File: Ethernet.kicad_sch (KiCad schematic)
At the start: 40 parts, among them U4 LAN8742A

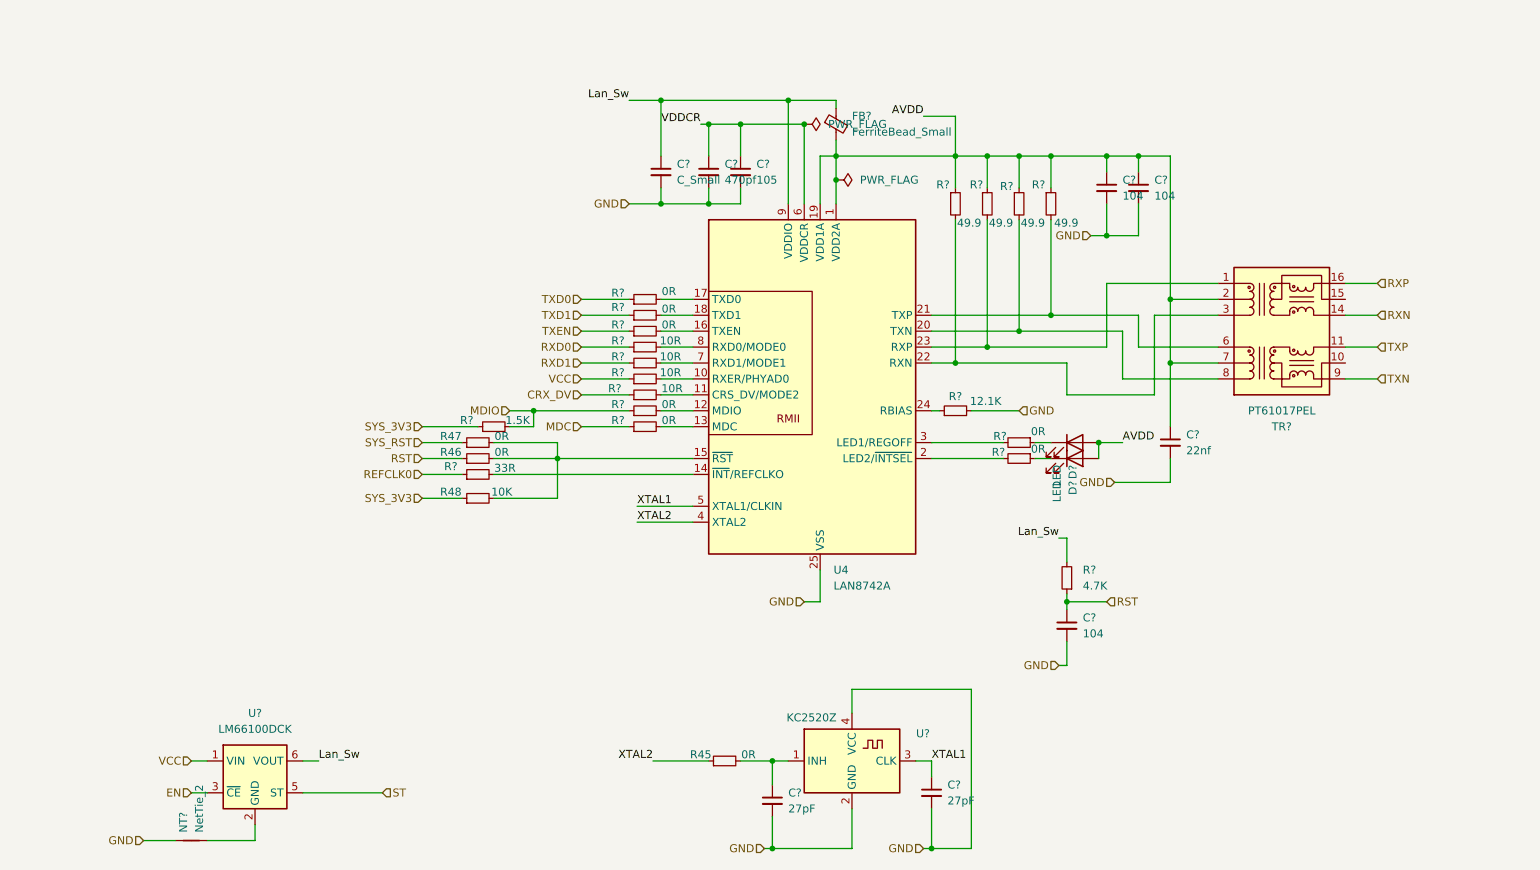
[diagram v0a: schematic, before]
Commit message: Completed ETH Module as per ref schematic also populated compatible busses in processor module
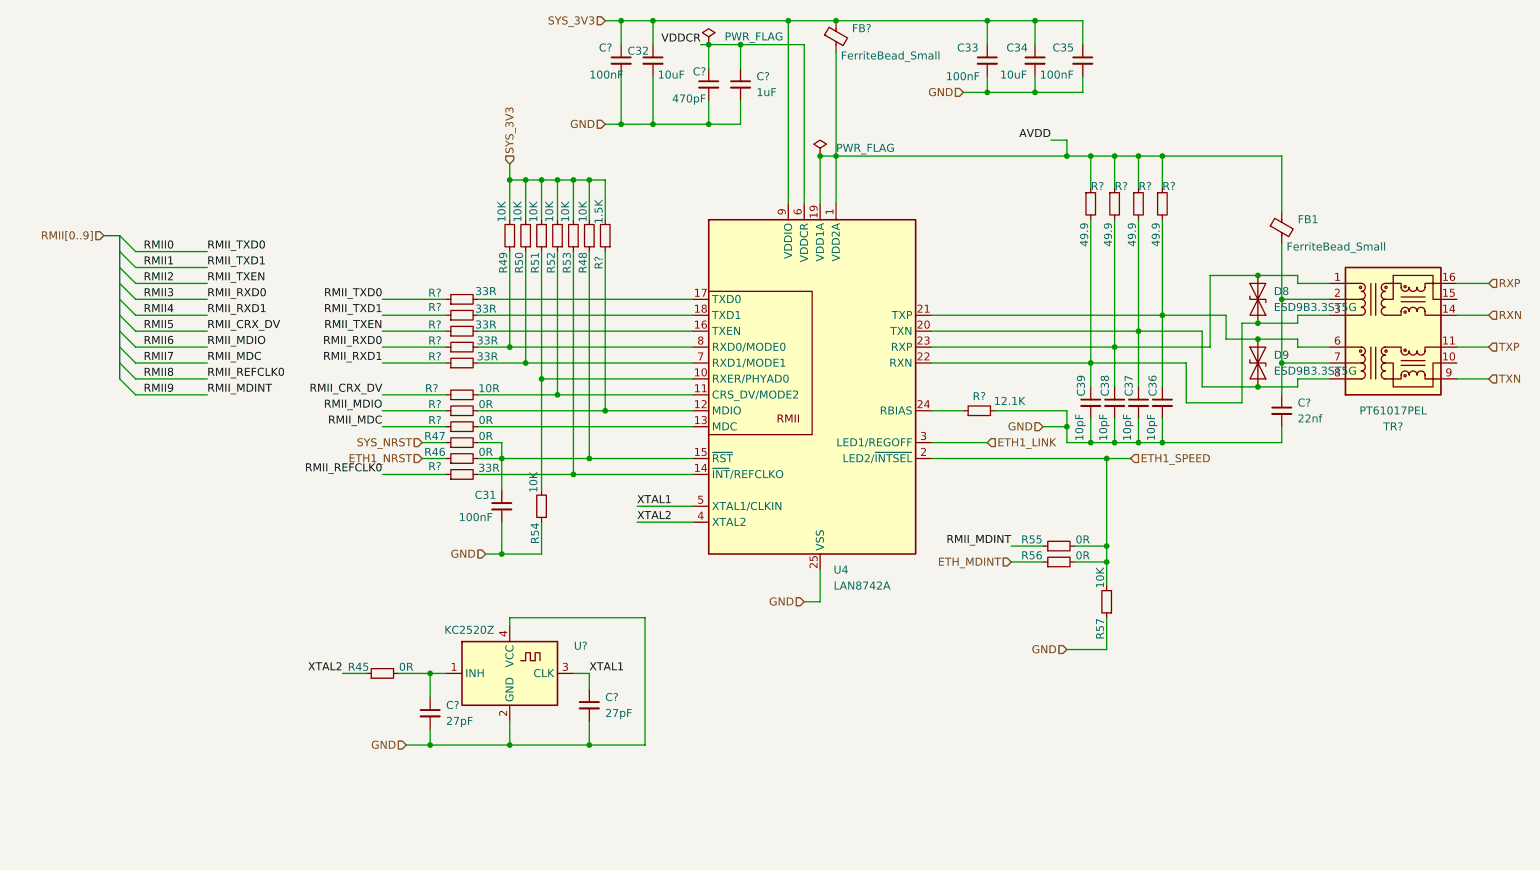
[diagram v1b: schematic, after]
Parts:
- removed C? (x3): 104, Capacitor_SMD:C_0603_1608Metric_Pad1.08x0.95mm_HandSolder, symbol Device:C_Small
- removed D? (x2): LED, LED_SMD:LED_0603_1608Metric, symbol Device:LED
- removed NT?: NetTie_2, NetTie:NetTie-2_SMD_Pad0.5mm, symbol Device:NetTie_2
- removed R? (x2): 0R, Resistor_SMD:R_0603_1608Metric_Pad0.98x0.95mm_HandSolder, symbol Device:R_Small
- removed R?: 10R, Resistor_SMD:R_0603_1608Metric_Pad0.98x0.95mm_HandSolder, symbol Device:R_Small
- removed R?: 4.7K, Resistor_SMD:R_0603_1608Metric_Pad0.98x0.95mm_HandSolder, symbol Device:R_Small
- removed U?: LM66100DCK, Package_TO_SOT_SMD:SOT-363_SC-70-6, symbol Power_Management:LM66100DCK
- added C31, C33, C35: 100nF, Capacitor_SMD:C_0603_1608Metric_Pad1.08x0.95mm_HandSolder, symbol Device:C_Small
- added C32, C34: 10uF, Capacitor_SMD:C_0603_1608Metric_Pad1.08x0.95mm_HandSolder, symbol Device:C_Small
- added C36, C37, C38, C39: 10pF, Capacitor_SMD:C_0603_1608Metric_Pad1.08x0.95mm_HandSolder, symbol Device:C_Small
- added D8, D9: ESD9B3.3ST5G, Diode_SMD:D_SOD-923, symbol Diode:ESD9B3.3ST5G
- added FB1: FerriteBead_Small, Inductor_SMD:L_Walsin_WLFM252009x, symbol Device:FerriteBead_Small
- added R49, R50, R51, R52, R53, R54, R57: 10K, Resistor_SMD:R_0603_1608Metric_Pad0.98x0.95mm_HandSolder, symbol Device:R_Small
- added R55, R56: 0R, Resistor_SMD:R_0603_1608Metric_Pad0.98x0.95mm_HandSolder, symbol Device:R_Small
- C?: value C_Small -> 100nF
- C?: value 105 -> 1uF
- C?: value 470pf -> 470pF
- R? (x3): value 0R -> 33R
- R? (x2): value 10R -> 33R
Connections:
- net Lan_Sw is gone; now on net SYS_3V3: C?.1, FB?.1, U4.9 (VDDIO)
- net AVDD: now also FB1.1; no longer C?.1, TR?.2 (C_TD), TR?.7 (C_RD)
- net GND: now also C31.2, C32.2, C33.2, C34.2, C35.2, C36.2, C37.2, C38.2, C39.2, R54.1, R57.1
- net SYS_3V3: now also R48.2, R?.2, C32.1, C33.1, C34.1, C35.1, R49.2, R50.2, R51.2, R52.2, R53.2; no longer R48.1, R?.1
- net at R?.2, U4.14 (~{INT}/REFCLKO): now also R53.1
- net at R?.2, TR?.1 (TD+), U4.23 (RXP): now also C38.1, D8.2 (A2)
- net at R?.2, TR?.3 (TD-), U4.22 (RXN): now also C39.1, D8.1 (A1)
- net at R?.2, TR?.6 (RD+), U4.21 (TXP): now also C36.1, D9.2 (A2)
- net at R?.2, TR?.8 (RD-), U4.20 (TXN): now also C37.1, D9.1 (A1)
- net at R46.2, R47.2, U4.15 (~{RST}): now also R48.1, C31.1; no longer R48.2
- net ETH1_LINK: now reaches U4.3 (LED1/REGOFF)
- net at U4.10 (RXER/PHYAD0): now also R51.1, R54.2
- net at R?.2, U4.7 (RXD1/MODE1): now also R50.1
- net at R?.2, U4.8 (RXD0/MODE0): now also R49.1
- net at R?.2, U4.12 (MDIO): now also R?.1
- net ETH1_SPEED: now reaches U4.2 (LED2/~{INTSEL})
- net ETH1_SPEED: now also R55.2, R56.2, R57.2
- net at R?.2, U4.11 (CRS_DV/MODE2): now also R52.1
- net CRX_DV renamed RMII5
- net MDC renamed RMII7
- net MDIO renamed RMII6
- net RMII6: no longer R?.2
- net REFCLK0 renamed RMII8
- net RST renamed ETH1_NRST
- net RXD0 renamed RMII3
- net RXD1 renamed RMII4
- net SYS_RST renamed SYS_NRST
- net TXD0 renamed RMII0
- net TXD1 renamed RMII1
- net TXEN renamed RMII2
- new net: C?.1, FB1.2, TR?.2 (C_TD), TR?.7 (C_RD)
- new net ETH_MDINT: R56.1
- new net RMII9: R55.1
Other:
- moved on the sheet: C?, FB?, R45, R46, R47, R48, R?, TR?, U?

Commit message: Updated Processor With ETH Pins
Also updated Capacitors and Resistors to 402
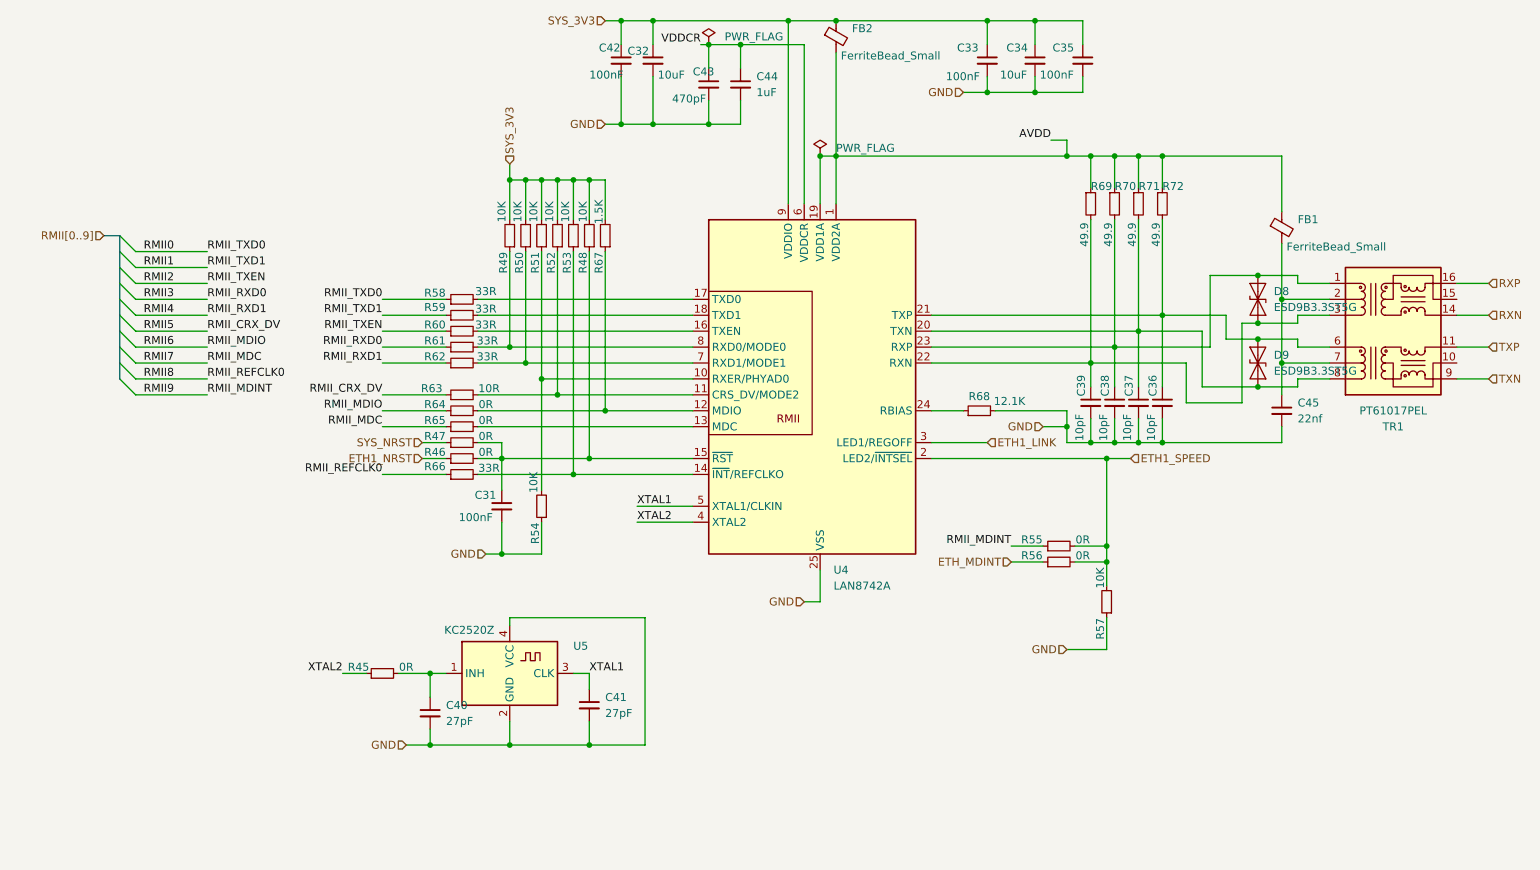
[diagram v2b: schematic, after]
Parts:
- C31, C32, C33, C34, C35, C36, C37, C38, C39: footprint Capacitor_SMD:C_0603_1608Metric_Pad1.08x0.95mm_HandSolder -> Capacitor_SMD:C_0402_1005Metric
- C40, C41, C42, C43, C44, C45: renamed from C?; footprint Capacitor_SMD:C_0603_1608Metric_Pad1.08x0.95mm_HandSolder -> Capacitor_SMD:C_0402_1005Metric
- R45, R46, R47, R48, R49, R50, R51, R52, R53, R54, R55, R56, R57: footprint Resistor_SMD:R_0603_1608Metric_Pad0.98x0.95mm_HandSolder -> Resistor_SMD:R_0402_1005Metric
- R58, R59, R60, R61, R62, R63, R64, R65, R66, R67, R68, R69, R70, R71, R72: renamed from R?; footprint Resistor_SMD:R_0603_1608Metric_Pad0.98x0.95mm_HandSolder -> Resistor_SMD:R_0402_1005Metric
- gave numbers to parts that had none: 3
